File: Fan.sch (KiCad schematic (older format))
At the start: 9 parts

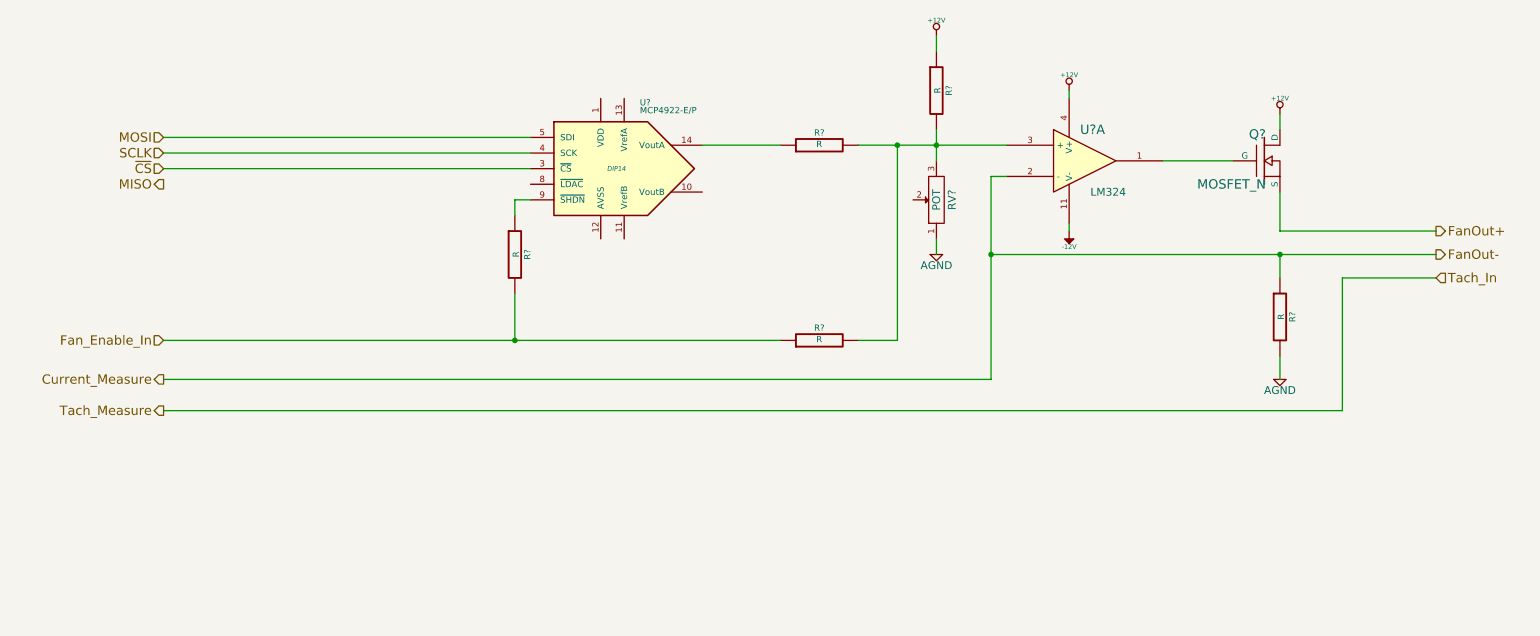
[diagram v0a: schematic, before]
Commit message: Fan/Current Module Refactor
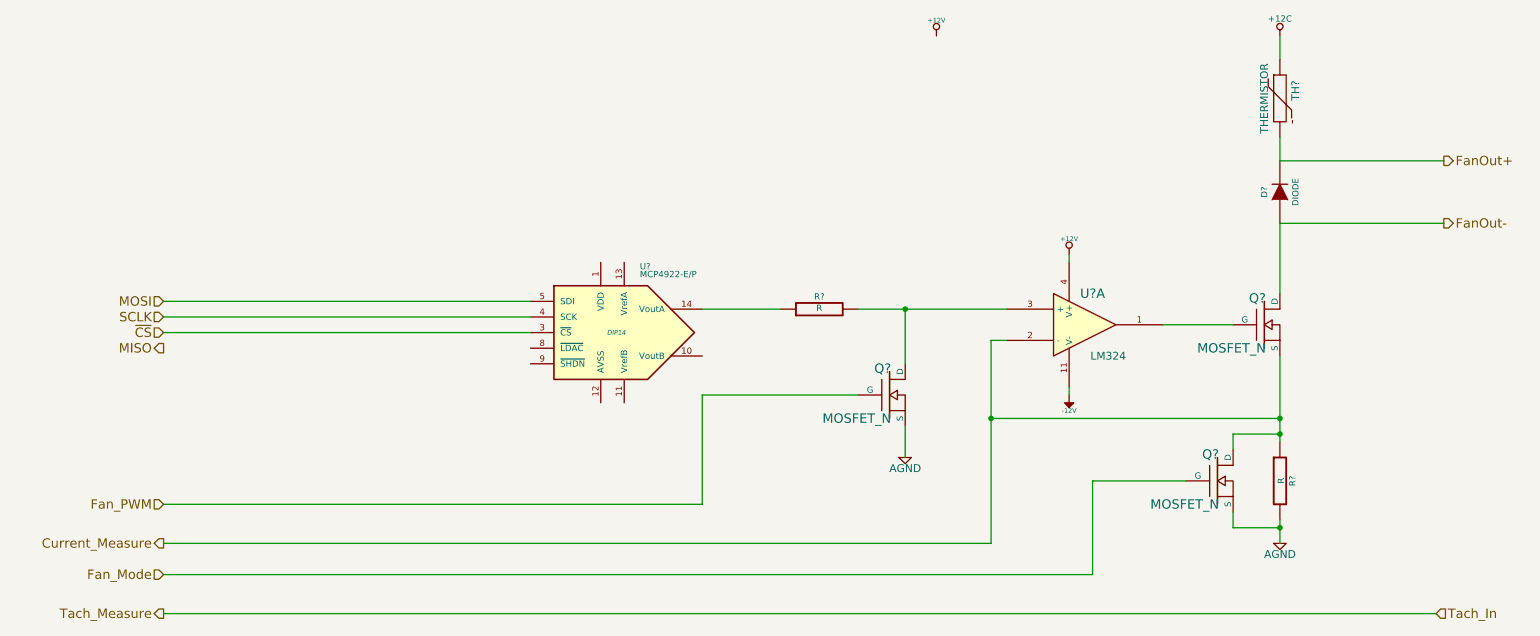
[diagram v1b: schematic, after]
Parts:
- removed R? (x3): R, ~, symbol R
- removed RV?: POT, ~, symbol POT
- added D?: DIODE, ~, symbol DIODE
- added Q? (x2): MOSFET_N, ~, symbol MOSFET_N
- added TH?: THERMISTOR, ~, symbol THERMISTOR
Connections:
- net +12V: no longer Q?.D
- net AGND: now also Q?.S, Q?.S
- net Current_Measure: now also Q?.S, Q?.D
- net FanOut+: now also D?.2 (K), TH?.2; no longer Q?.S
- net at R?.2, U?.3 (+): now also Q?.D
- new net +12C: TH?.1
- new net FanOut-: D?.1 (A), Q?.D
- new net Fan_Mode: Q?.G
- new net Fan_PWM: Q?.G
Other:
- moved on the sheet: Q?, R?, U?, U?A
